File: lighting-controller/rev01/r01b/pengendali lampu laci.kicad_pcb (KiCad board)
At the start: 2 copper layers, 94 x 54 mm, 20 parts, among them M1 LM2596_Module, P1 Power, SW1 SPST

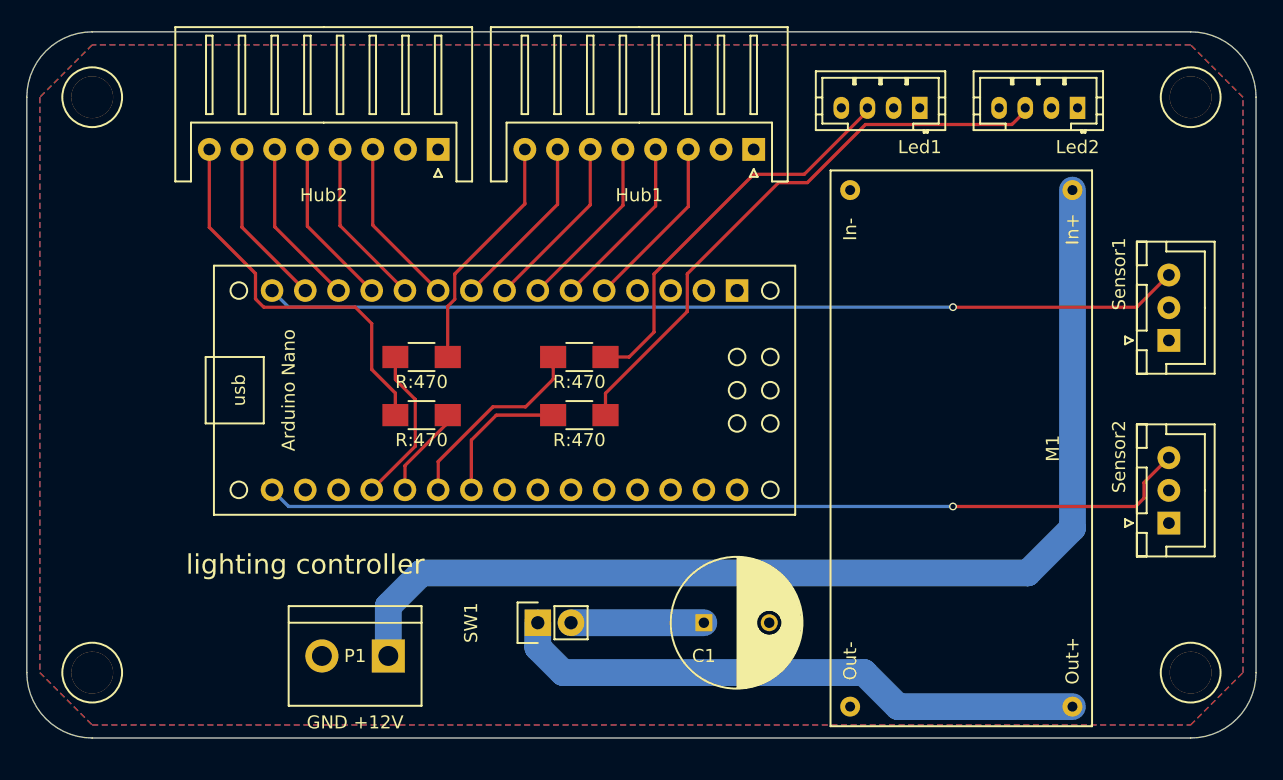
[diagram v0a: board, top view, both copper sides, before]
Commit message: Update controller
* Add led
* Use switch
* Use barrel jack
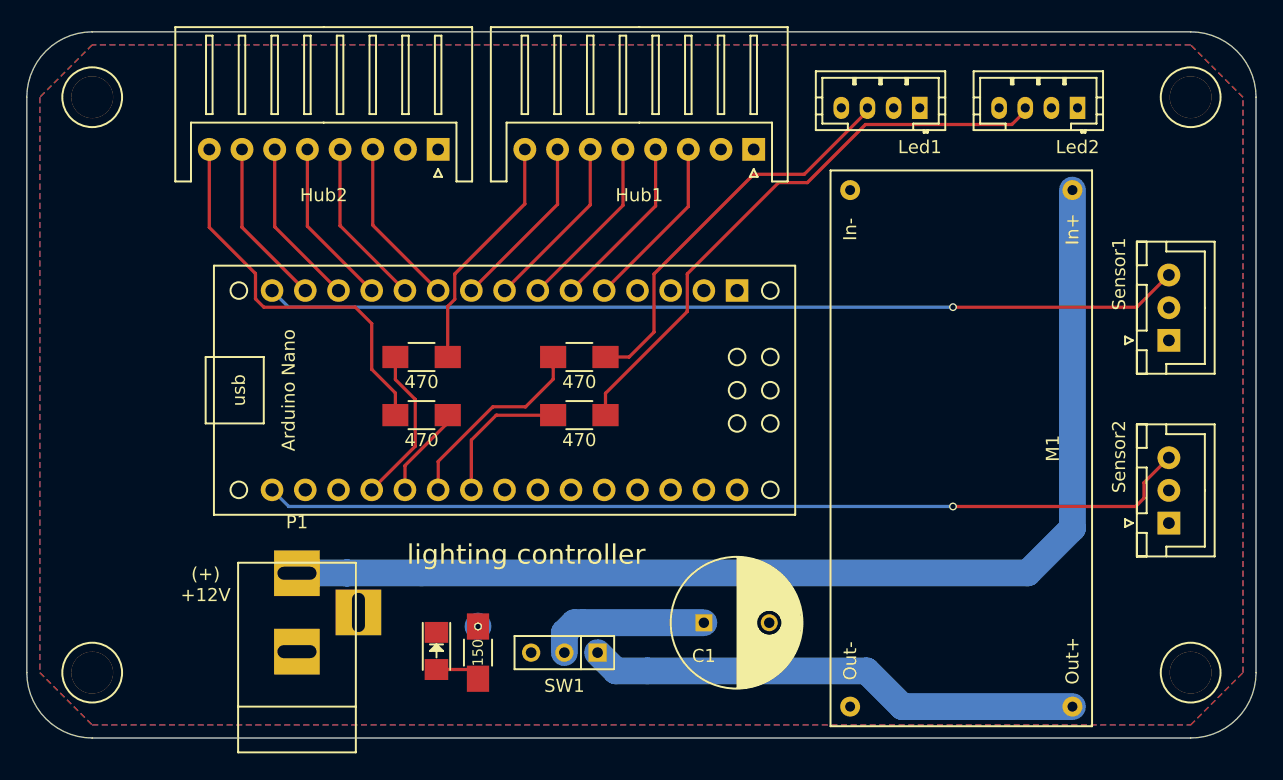
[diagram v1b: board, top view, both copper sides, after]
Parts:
- added D1: LED, LEDs:LED_1206, F.Cu at (84.3, 85.3)
- added R5: 150, Resistors_SMD:R_1206_HandSoldering, F.Cu at (87.5, 85.5)
- P1: footprint Connect:bornier2 -> Connect:BARREL_JACK
- R1, R2, R3, R4: value R:470 -> 470
- SW1: footprint Pin_Headers:Pin_Header_Straight_1x02 -> Buttons_Switches_ThroughHole:SW_Micro_SPST
- moved P1 4.45 mm to (73.7, 85.6), turned to 90 degrees
- moved SW1 3.06 mm to (94.1, 85.5), turned to 180 degrees
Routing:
- net /Vreg: track 44.6 -> 38.0 mm
- net Net-(D1-Pad2): track 0.00 -> 3.47 mm
- net +5V: track 10.2 -> 12.5 mm, vias 0 -> 1
- net VCC: track 84.4 -> 86.6 mm
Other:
- board text added: "(+) +12V"
- board text added: "FAJRAN 2016"
- board text added: "REV 01"
- board text removed: "GND +12V"
- board text removed: "fajran 2016"
- board text removed: "rev01"
